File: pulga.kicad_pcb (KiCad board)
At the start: 2 copper layers, 38 x 34.1 mm, 31 parts, among them J1 Conn_01x04_Pin, SW1 SW_Push, SW2 SW_Push, U2 ESP32-C3-WROOM-02, U3 TCAN332G, U4 AMS1117-3.3

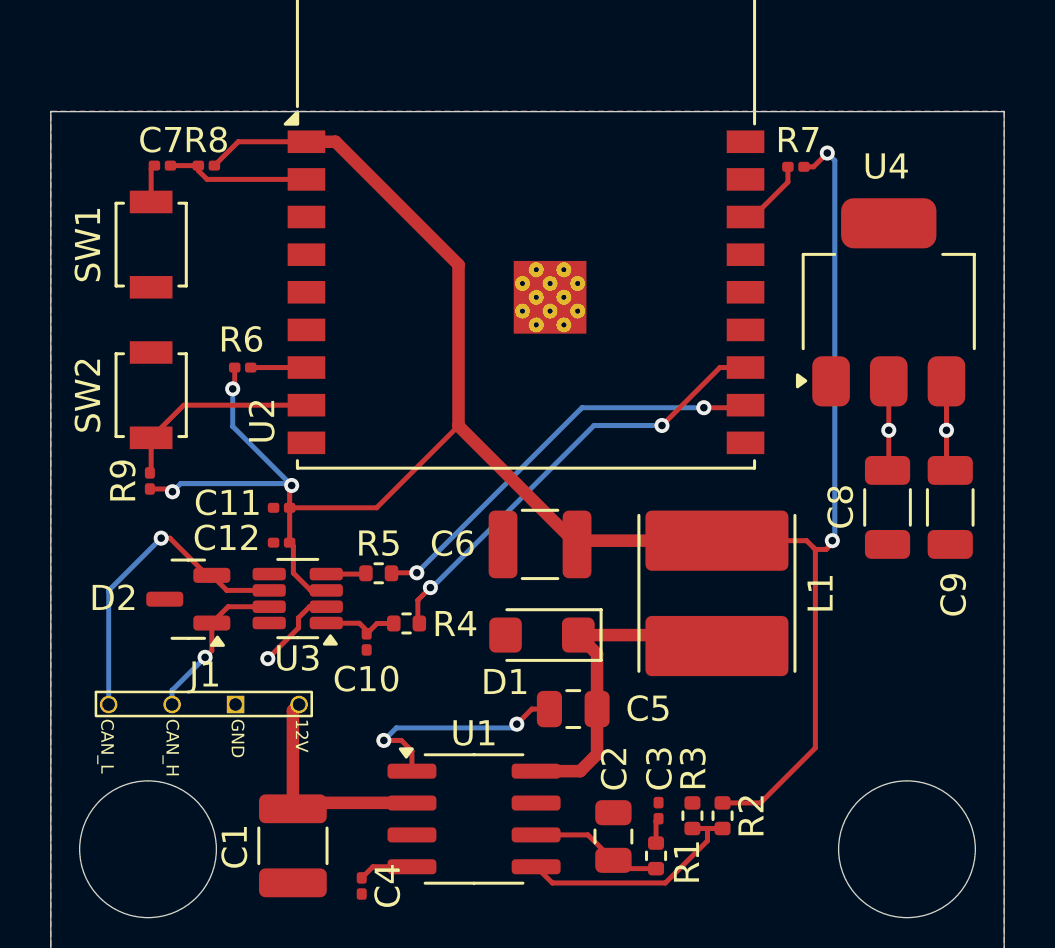
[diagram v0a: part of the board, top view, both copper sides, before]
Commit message: adicionando as conexões 5v, GND, USB_(P|N) e o LDO
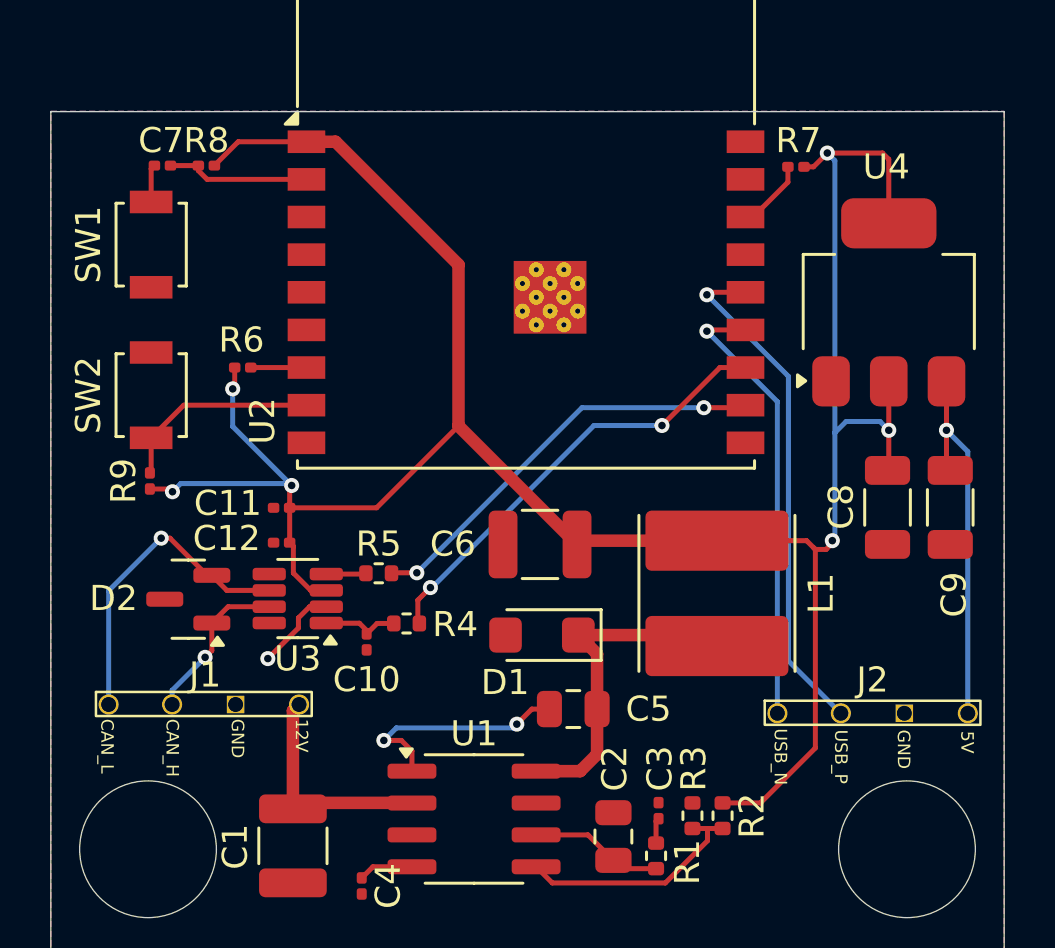
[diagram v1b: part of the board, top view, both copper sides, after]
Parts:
- added J2: Conn_01x04_Pin, through_hole:obd_main_pins, F.Cu at (125.4, 72.3)
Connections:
- U2 pad 13: unconnected-(U2-IO18-Pad13) -> usb_n
- U2 pad 14: unconnected-(U2-IO19-Pad14) -> usb_p
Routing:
- net usb_p: track 0.00 -> 20.5 mm, vias 0 -> 1
- net usb_n: track 0.00 -> 18.0 mm, vias 0 -> 1
- net 5V: track 3.61 -> 15.2 mm
- net 3V3: track 93.9 -> 101.5 mm

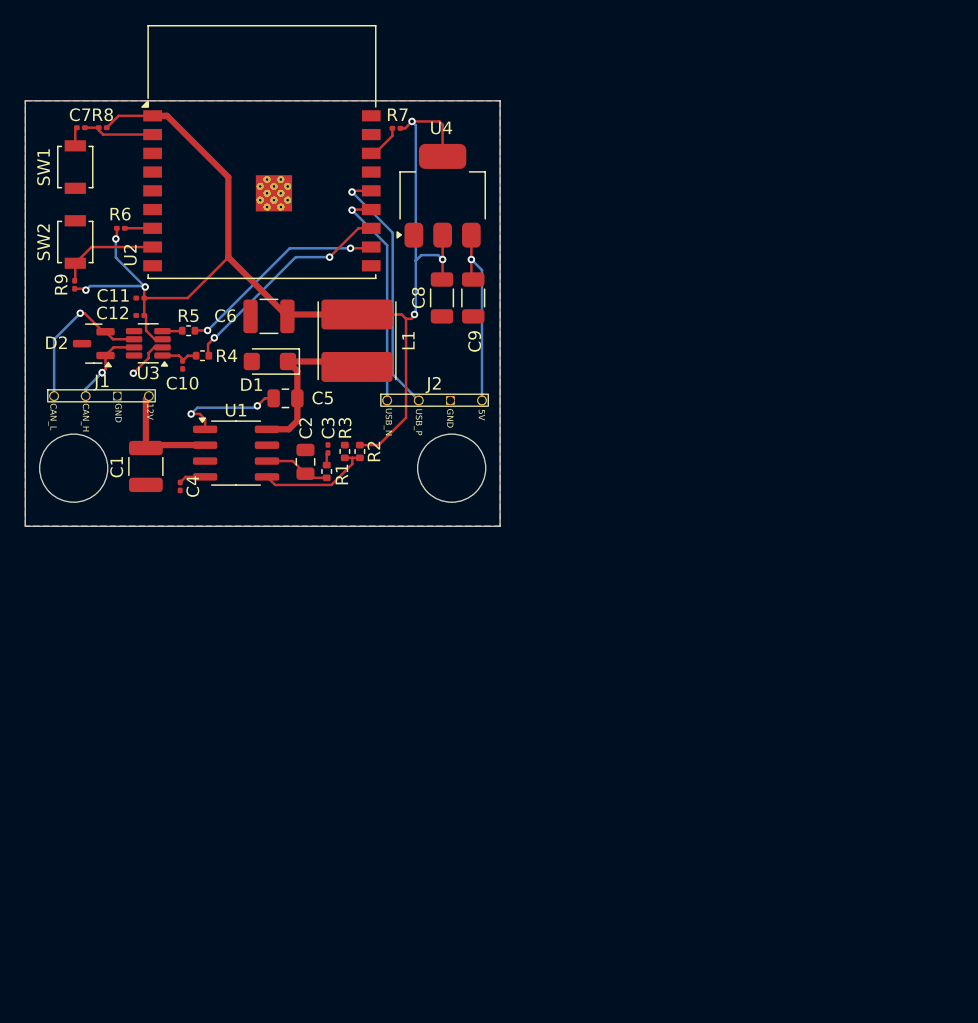
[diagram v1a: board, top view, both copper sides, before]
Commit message: centralizando o módulo na folha de PCB e dando nomes as partes no SCH
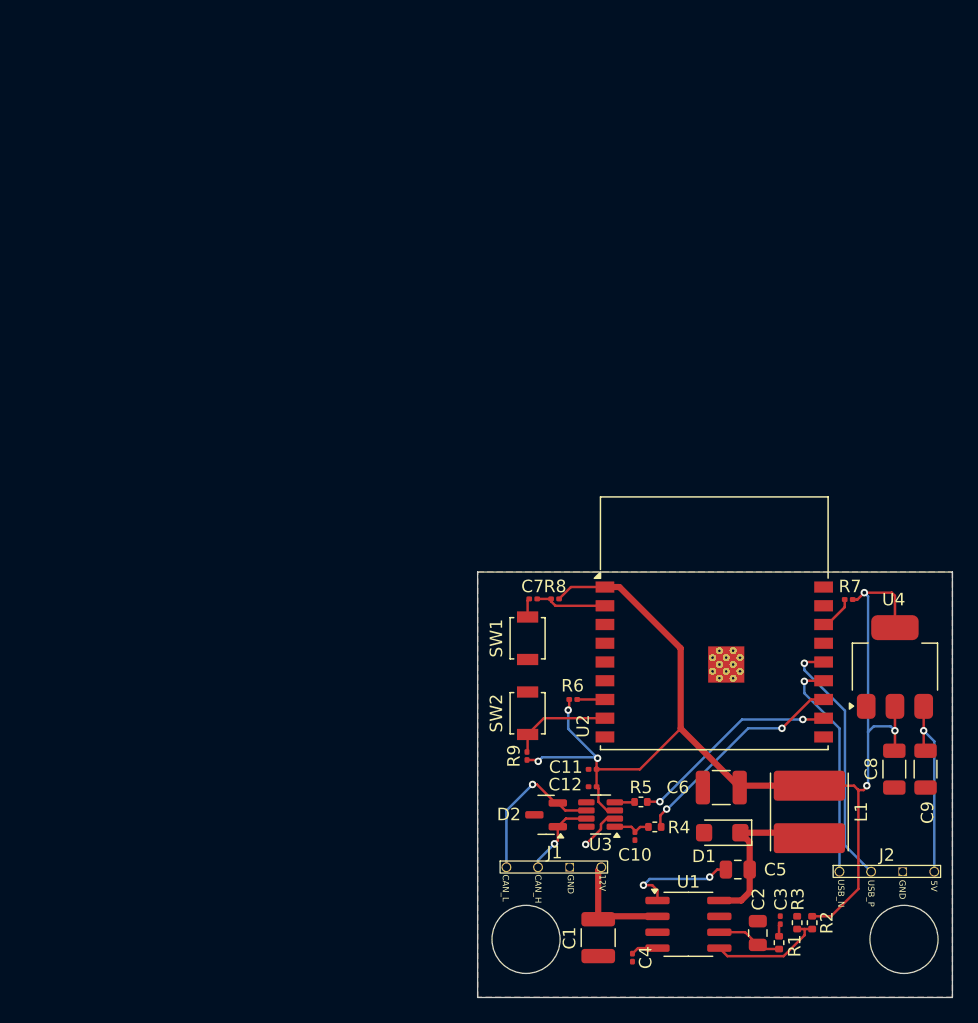
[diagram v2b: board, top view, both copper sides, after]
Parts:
- moved C9 52.3 mm to (164.7, 99.3)
- moved C11 52.3 mm to (138.0, 99.4)
- moved C12 52.3 mm to (138.0, 100.7)
- moved C7 52.3 mm to (133.3, 85.7)
- moved C8 52.3 mm to (162.2, 99.3)
- moved D2 52.3 mm to (134.3, 103.0)
- moved R5 52.3 mm to (141.9, 102.0)
- moved R7 52.3 mm to (158.5, 85.8)
- moved R8 52.3 mm to (135.0, 85.7)
- moved R9 52.3 mm to (132.8, 98.3)
- moved C1 52.3 mm to (138.5, 112.8)
- moved C10 52.3 mm to (141.4, 104.7)
- moved C3 52.3 mm to (153.0, 111.4)
- moved C5 52.3 mm to (149.6, 107.4)
- moved C6 52.3 mm to (148.3, 100.8)
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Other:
- board size 38 x 34.1 mm -> 38 x 34 mm

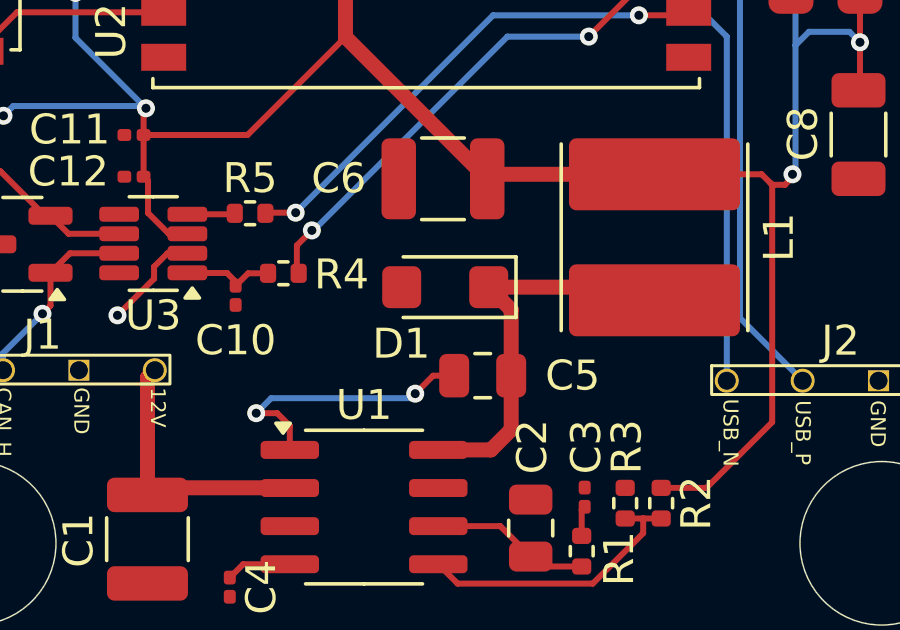
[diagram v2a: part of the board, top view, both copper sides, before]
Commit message: adicionando o LCSC aos componentes do circuito de alimentação 12V-3.3V
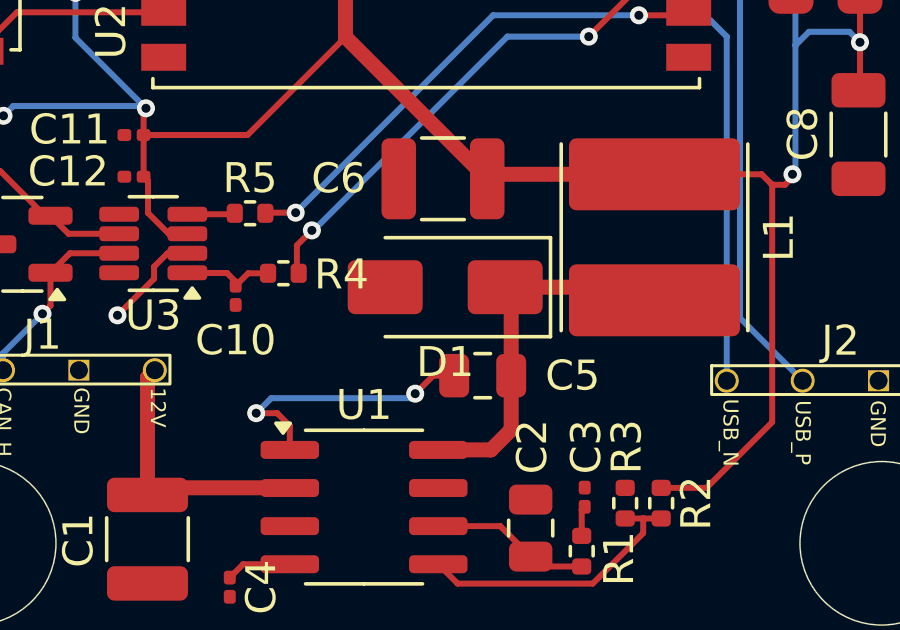
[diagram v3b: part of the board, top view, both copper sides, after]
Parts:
- D1: footprint Diode_SMD:D_SMF -> Diode_SMD:D_SMA

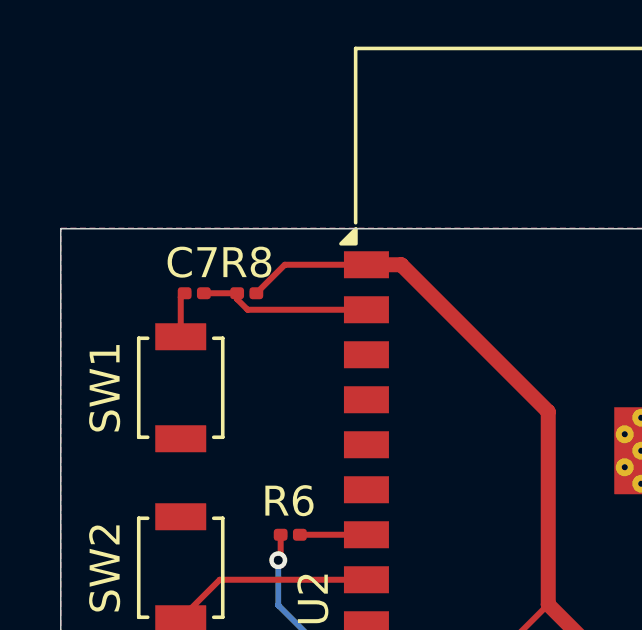
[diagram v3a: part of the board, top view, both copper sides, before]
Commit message: corrigindo a posição de C7 para ficar em paralelo em relação a SW1
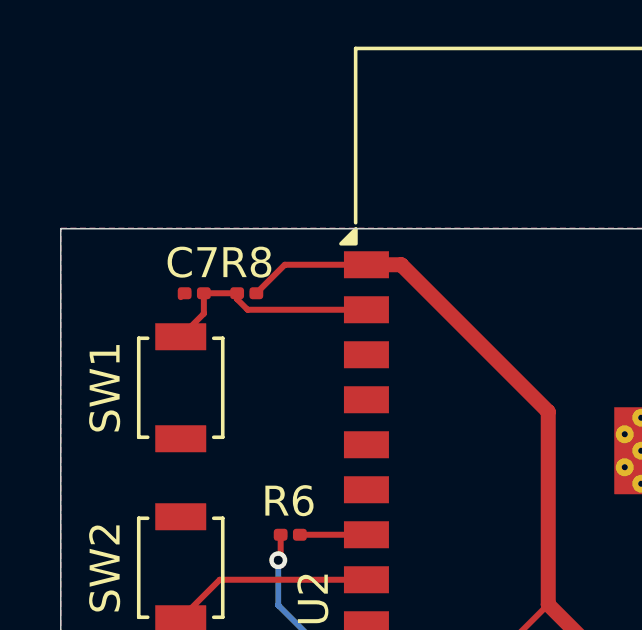
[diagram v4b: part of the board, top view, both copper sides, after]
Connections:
- C7 pad 2: Net-(C7-Pad2) -> GND
- SW1 pad 2: Net-(C7-Pad2) -> chip_en
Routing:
- net chip_en: track 5.76 -> 7.53 mm
- net Net-(C7-Pad2): track 1.50 -> 0.00 mm

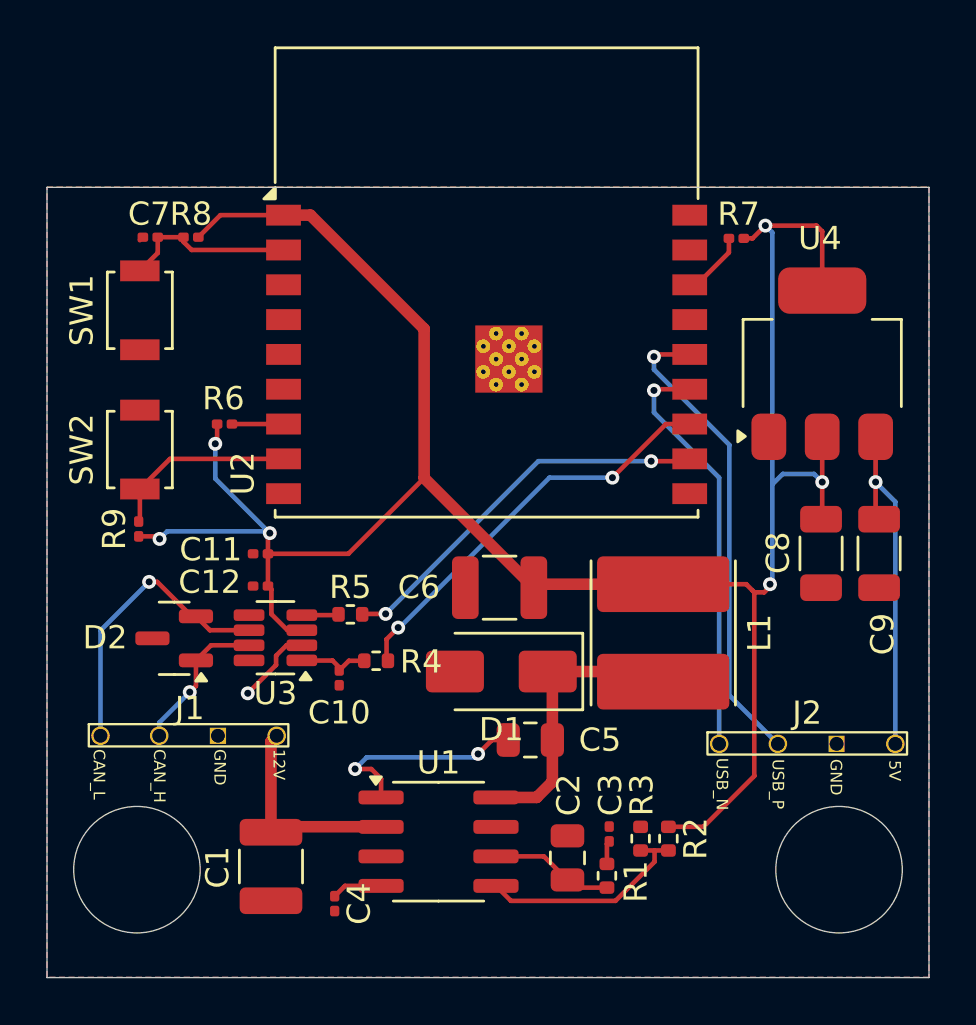
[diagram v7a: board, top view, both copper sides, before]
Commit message: invertendo a posição do circuito can e ldo; trocando 2 conectores de 4 vias por 4 de 2 vias
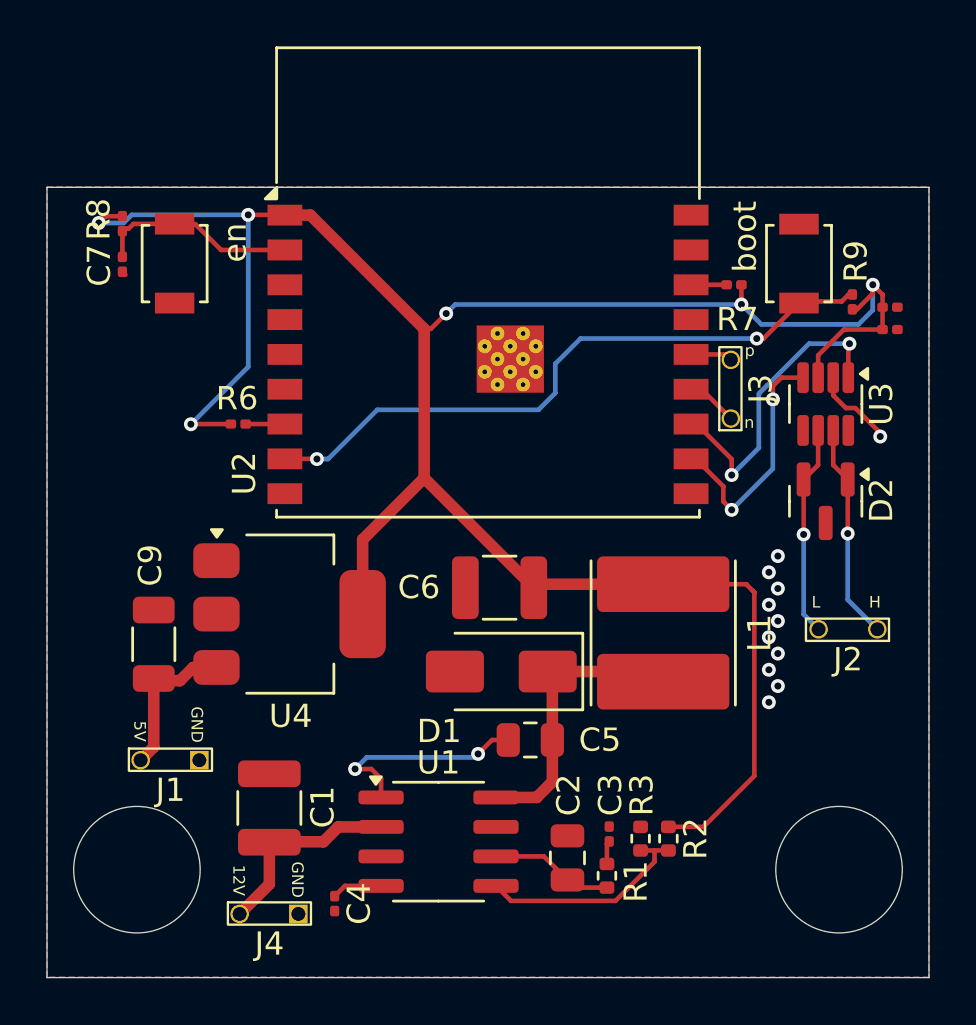
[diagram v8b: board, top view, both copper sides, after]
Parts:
- removed C10: 1u, Capacitor_SMD:C_0201_0603Metric
- removed C8: 22u, Capacitor_SMD:C_1206_3216Metric
- removed R4, R5: 1k, Resistor_SMD:R_0402_1005Metric
- added J3: Conn_01x02_Socket, through_hole:two_th_pins, F.Cu at (160.1, 92.2)
- added J4: Conn_01x02_Socket, through_hole:two_th_pins, F.Cu at (138.4, 116.7)
- J1, J2: value Conn_01x04_Pin -> Conn_01x02_Socket; footprint through_hole:obd_main_pins -> through_hole:two_th_pins
- moved R9 32.3 mm to (163.5, 88.5)
- moved C9 31.5 mm to (133.4, 103.2), turned to 90 degrees
- moved C12 29.7 mm to (165.1, 88.7), turned to 180 degrees
- moved boot 29.5 mm to (161.2, 86.8)
- moved C11 28.8 mm to (165.1, 89.7), turned to 180 degrees
- moved D2 28.7 mm to (162.3, 97.1), turned to -90 degrees
- moved U3 25.8 mm to (162.3, 92.9), turned to -90 degrees
- moved U4 25.4 mm to (139.2, 102.0), turned to 0 degrees
- moved J2 9.33 mm to (163.3, 100.8), turned to 180 degrees
- moved R8 3.01 mm to (132.1, 85.1), turned to -90 degrees
- moved C1 2.52 mm to (138.4, 110.3), turned to 90 degrees
- moved en 2.51 mm to (134.3, 86.8)
- moved R7 2.00 mm to (158.4, 87.8)
- moved C7 1.67 mm to (132.1, 86.9), turned to -90 degrees
- moved J1 0.88 mm to (134.1, 110.0)
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- renumbered SW2 to boot, SW1 to en
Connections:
- J1 pad 1: 12V -> 5V
- J2 pad 1: 5V -> can_h
- J2 pad 2: GND -> can_l
- U3 pad 1: Net-(U3-TXD) -> esp32_tx
- U3 pad 4: Net-(U3-RXD) -> esp32_rx
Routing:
- net boot: track 8.15 -> 28.2 mm, vias 0 -> 2
- net usb_p: track 20.5 -> 1.87 mm, vias 1 -> 0
- net usb_n: track 18.0 -> 2.30 mm, vias 1 -> 0
- net 5V: track 15.2 -> 6.73 mm, vias 1 -> 0
- net esp32_rx: track 16.9 -> 11.1 mm
- net esp32_tx: track 17.9 -> 13.4 mm
- net can_l: track 12.7 -> 9.09 mm
- net Net-(U3-TXD): track 3.12 -> 0.00 mm
- net can_h: track 6.51 -> 9.35 mm
- net Net-(U3-RXD): track 1.59 -> 0.00 mm
- net Net-(U2-IO2): track 2.88 -> 1.59 mm
- net chip_en: track 7.53 -> 8.64 mm
- net Net-(U2-IO8): track 2.22 -> 1.63 mm
- net GND: track 3.60 -> 3.80 mm, vias 1 -> 11
